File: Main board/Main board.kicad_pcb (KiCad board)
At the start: 4 copper layers, 79 x 79 mm, 120 parts, among them CN1 PA001-4P, CN2 PA001-4P, J1 TagConnect_TC2030-NL, J2 Conn_01x02_Pin, J3 Conn_01x02_Pin, J5 Connector, USB-TYPE-C-16P, J6 436500201, J7 Conn_01x04_Pin, Q1 SI7232DN-T1-GE3, Q2 SI7232DN-T1-GE3, SW1 SKRKAEE020, SW2 SKRKAEE020, U1 STM32U575VGTx, U10 TLV75733PDBV, U11 NRVB120VLSFT1G, U12 NRVB120VLSFT1G, U2 TPS62901RPJR, U3 MS5607-02BA03, U4 ADXL375BCCZ-RL7, U5 SN74LVC1G32MDBVREP, U6 MMC5983MA, U7 SN74AHCT125DR, U9 ICM-45686, X1 1XXD32000MBA, Y1 ECS-327TXO-33-TR

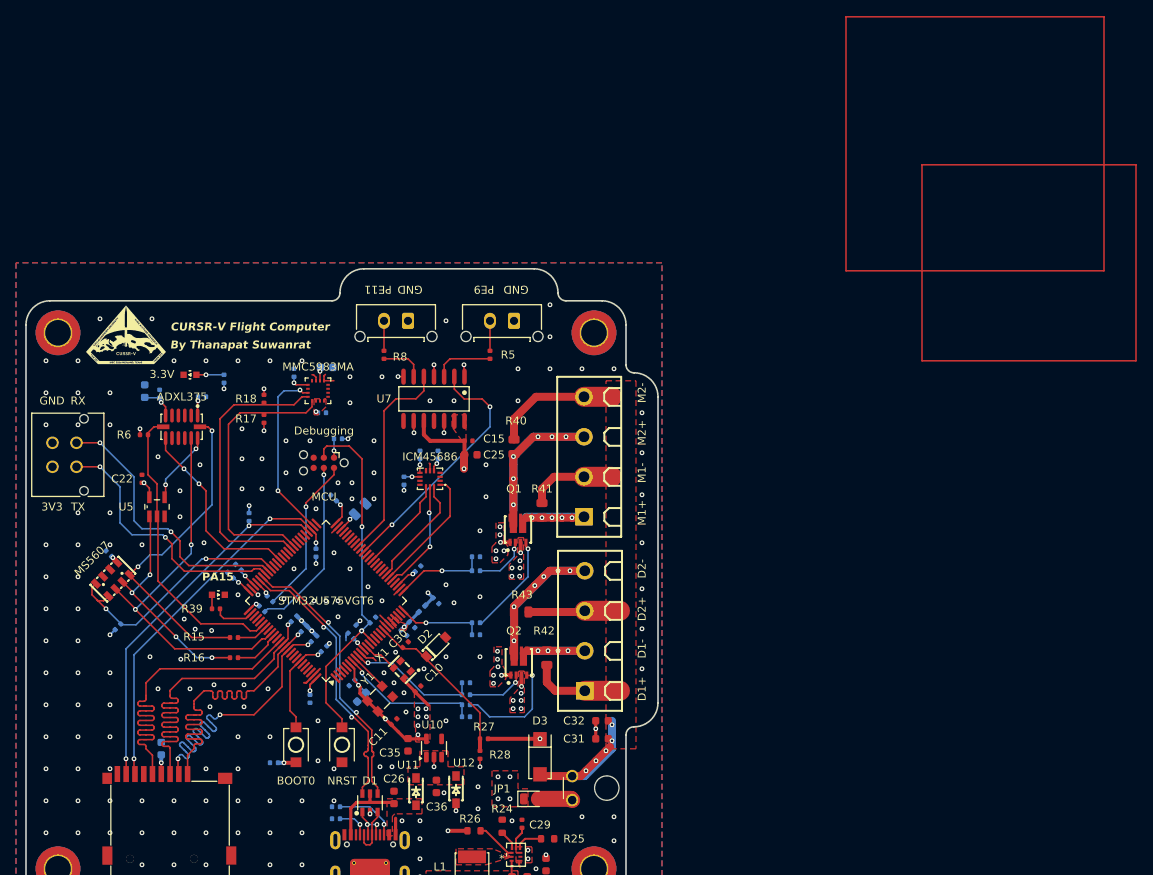
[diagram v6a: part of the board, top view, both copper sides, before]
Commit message: Included IMU project
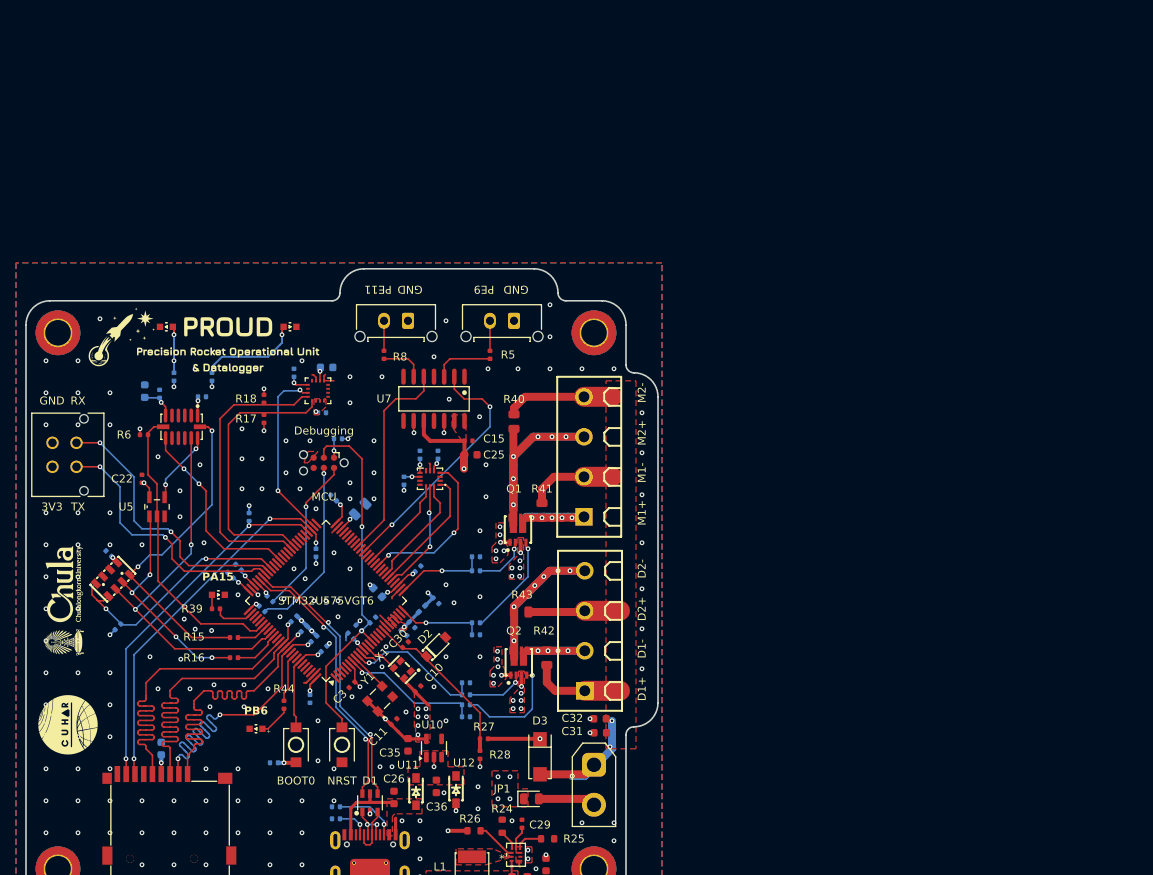
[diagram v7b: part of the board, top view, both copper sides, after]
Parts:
- removed the G*** at (125.0, 66.8)
- added D6: Yellow, LEDDD:WL-SMCW_0603, F.Cu at (141.2, 116.0)
- added D7: GREEN, LEDDD:WL-SMCW_0603, F.Cu at (145.5, 65.8)
- added G***: LOGO, LOGO, F.Cu at (117.2, 100.0)
- added G***: LOGO, LOGO, F.Cu at (124.2, 67.2)
- added G***: LOGO, LOGO, F.Cu at (117.8, 115.5)
- added G***: LOGO, LOGO, F.Cu at (137.8, 68.0)
- added G***: LOGO, LOGO, B.Cu at (126.5, 125.8)
- added R29: 470Ω, PCM_JLCPCB:R_0402, B.Cu at (135.8, 72.0)
- added R44: 470Ω, PCM_JLCPCB:R_0402, F.Cu at (144.8, 113.0)
- C3: moved to F.Cu
- J6: footprint molex1x03:CONN_SD-43650-001_02_MOL -> Connector_AMASS:AMASS_XT30UPB-F_1x02_P5.0mm_Vertical
- moved C1 13.3 mm to (156.4, 98.9), turned to 135 degrees
- moved D4 6.69 mm to (130.1, 65.8)
- moved R21 6.26 mm to (131.0, 72.0)
- moved R40 3.15 mm to (173.5, 77.6)
- moved J6 3.07 mm to (183.5, 120.5), turned to -90 degrees
- moved C31 0.78 mm to (184.3, 116.5)
- moved C32 0.35 mm to (184.2, 114.8)
- moved C3 0.25 mm to (153.2, 110.5)
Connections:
- R20 pad 1: +3V3 -> Net-(J1-VCC)
- R20 pad 2: Net-(J1-VCC) -> +3V3
- U1 pad 35: unconnected-(U1-PB0-Pad35) -> ICM_INT_1
- U1 pad 92: unconnected-(U1-PB6-Pad92) -> PB6
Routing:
- net ICM_INT_1: track 0.00 -> 20.4 mm, vias 0 -> 2
- net Net-(D7-A): track 0.00 -> 12.8 mm, vias 0 -> 1
- net PB6: track 0.00 -> 6.17 mm
- net PYRO+: track 70.6 -> 65.2 mm, vias 5 -> 3
- net Net-(D6-A): track 0.00 -> 4.03 mm
- net Net-(CN1-Pad3): track 35.1 -> 38.6 mm
- net Net-(D4-A): track 3.46 -> 5.81 mm
- net FIRE_C: track 16.5 -> 17.6 mm
- net +3V3: track 91.0 -> 90.1 mm, vias 37 -> 39
- net VBAT-: track 35.4 -> 34.5 mm, vias 178 -> 170
- net USB_DP: track 34.9 -> 34.3 mm
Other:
- board text added: "PB6"
- board text added: "R44"
- board text removed: "3.3V"
- board text removed: "ADXL375"
- board text removed: "By Thanapat Suwanrat"
- board text removed: "CURSR-V Flight Computer"
- board text removed: "ICM45686"
- board text removed: "MMC5983MA"
- board text removed: "MS5607"
- board text removed: "R21"
